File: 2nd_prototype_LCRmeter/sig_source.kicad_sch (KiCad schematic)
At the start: 19 parts, among them U13 MCP4561-502E_MS

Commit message: work on layout proto2
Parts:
- added C17: 10n, Capacitor_SMD:C_0603_1608Metric_Pad1.08x0.95mm_HandSolder, symbol Device:C
- added C56: 100n, Capacitor_SMD:C_0603_1608Metric_Pad1.08x0.95mm_HandSolder, symbol Device:C
- added JP3, JP4, JP5, JP6: SolderJumper_2_Open, Jumper:SolderJumper-2_P1.3mm_Open_RoundedPad1.0x1.5mm, symbol Jumper:SolderJumper_2_Open
- added TP20, TP21: TestPoint, Connector_Pin:Pin_D1.0mm_L10.0mm, symbol Connector:TestPoint
- added unit 5 of U18
- added U20: AD9837, Package_CSP:LFCSP-WD-10-1EP_3x3mm_P0.5mm_EP1.64x2.38mm, symbol Interface:AD9833xRM
- added X1: SG-210STF, Oscillator:Oscillator_SMD_SeikoEpson_SG210-4Pin_2.5x2.0mm, symbol Oscillator:SG-210STF
- U19: renamed from U13; footprint Snapeda:MCP4561-502E_MS_SOP65P490X110-8N -> Package_SO:MSOP-8_3x3mm_P0.65mm
- gave numbers to parts that had none: 1
- renumbered C17 to C51, C18 to C52, C20 to C53, C19 to C54, C21 to C55, JP1 to JP2, R10 to R56, R11 to R57, R9 to R58, R15 to R59, R13 to R60, R12 to R61, R14 to R62, U22 to U17
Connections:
- net +3V3: now also C17.1, U20.2 (VDD), X1.1 (~{ST}), X1.4 (Vcc)
- net +5V: now also U18.4 (V+)
- net -5V: now also U18.11 (V-)
- net F_Sync: now also U20.8 (~{FSYNC})
- net GND: now also C56.2, U20.4 (DGND), U20.9 (AGND), X1.2 (GND)
- net S_Clock: now also JP3.1 (A), JP6.2 (B); no longer U17.4 (SCLK)
- net S_Data: now also U20.6 (SDATA)
- net Sig_OUT: now also TP21.1
- net at U17.7 (OUT): now also JP5.1 (A); no longer U18.3 (+)
- new net: C17.2, U20.1 (COMP)
- new net: JP4.1 (A), U20.10 (VOUT)
- new net: C56.1, U20.3 (CAP/2.5V)
- new net: U20.5 (MCLK), X1.3 (OUT)
- new net: JP3.2 (B), U20.7 (SCLK)
- new net: JP4.2 (B), JP5.2 (B), TP20.1, U18.3 (+)
- new net: JP6.1 (A), U17.4 (SCLK)
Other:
- moved on the sheet: C51, C52, C53, C54, C55, JP2, R56, R57, R58, R59, R60, R61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

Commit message: finished final final_2
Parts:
- R57: value 33k -> 47k
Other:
- note added: "Zesílení na 3,42Vpp (+1,71V DC)"
- note added: "Škálování digitálním potenciometrem (8bit)"
- note removed: "Zesílení na 3Vpp (+1,5V DC)"
- note removed: "Škálování digitálním potenciometrem"
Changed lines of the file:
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@@
 		)
 	)
-	(text "Škálování digitálním \npotenciometrem"
+	(text "Škálování digitálním \npotenciometrem (8bit)"
 		(exclude_from_sim no)
 		(at 144.78 84.836 0)
@@
 		)
 	)
-	(text "Zesílení na 3Vpp (+1,5V DC)"
+	(text "Zesílení na 3,42Vpp (+1,71V DC)"
 		(exclude_from_sim no)
 		(at 119.634 99.314 0)
@@
 			)
 		)
-		(property "Value" "33k"
+		(property "Value" "47k"
 			(at 126.492 87.6299 90)
 			(effects

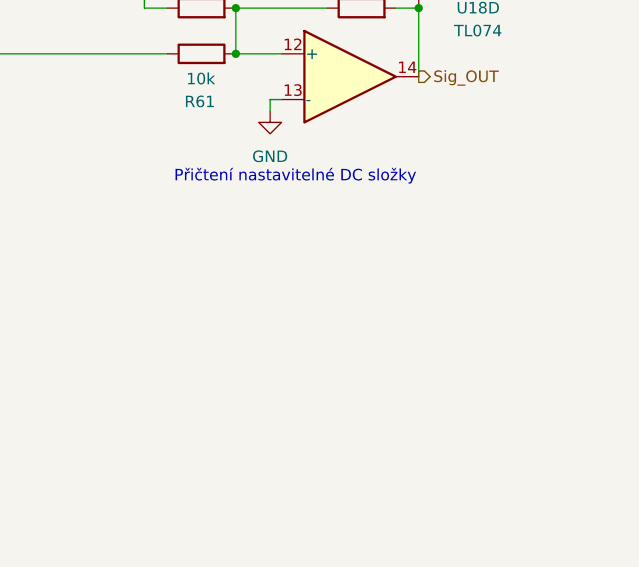
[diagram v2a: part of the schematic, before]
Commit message: Removed obsolete PDF files and updated LaTeX documents with new sections and references.
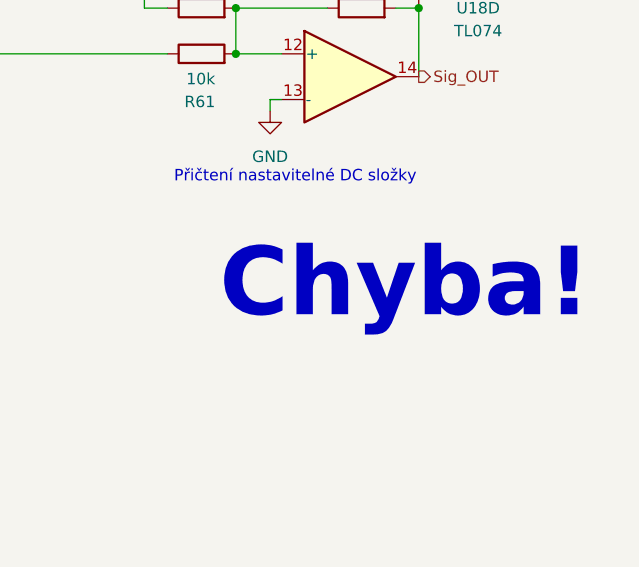
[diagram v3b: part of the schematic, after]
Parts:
- U17: value ~ -> (none)
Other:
- note added: "Chyba!"
